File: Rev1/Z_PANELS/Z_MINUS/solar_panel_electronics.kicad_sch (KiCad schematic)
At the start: 34 parts, among them U3 LTC3130EUDC-1-PBF

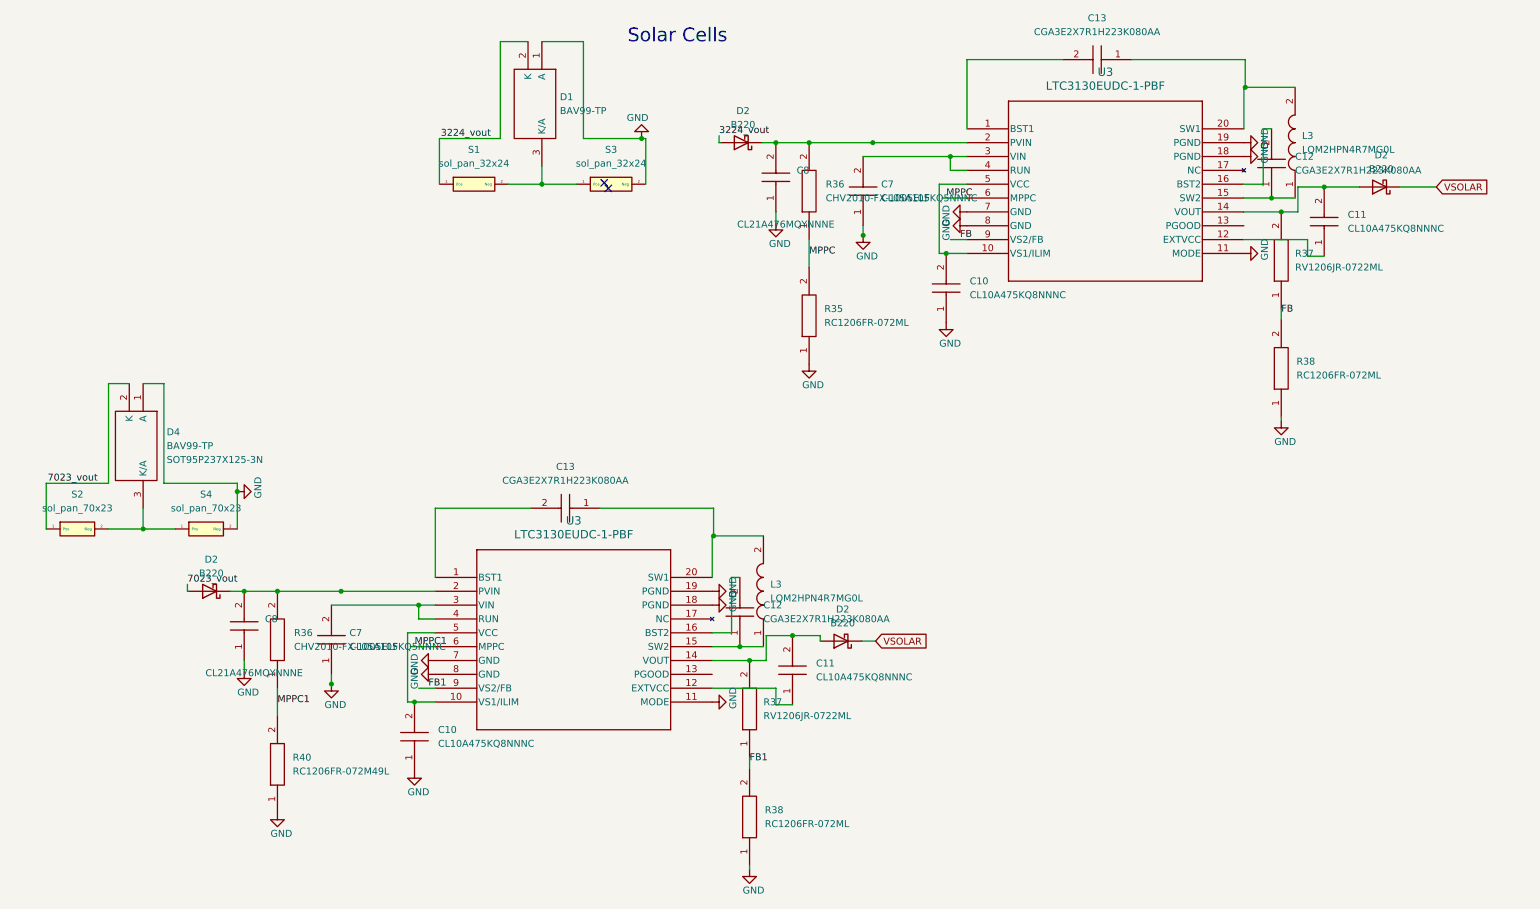
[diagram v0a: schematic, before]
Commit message: changed resistor sizes;
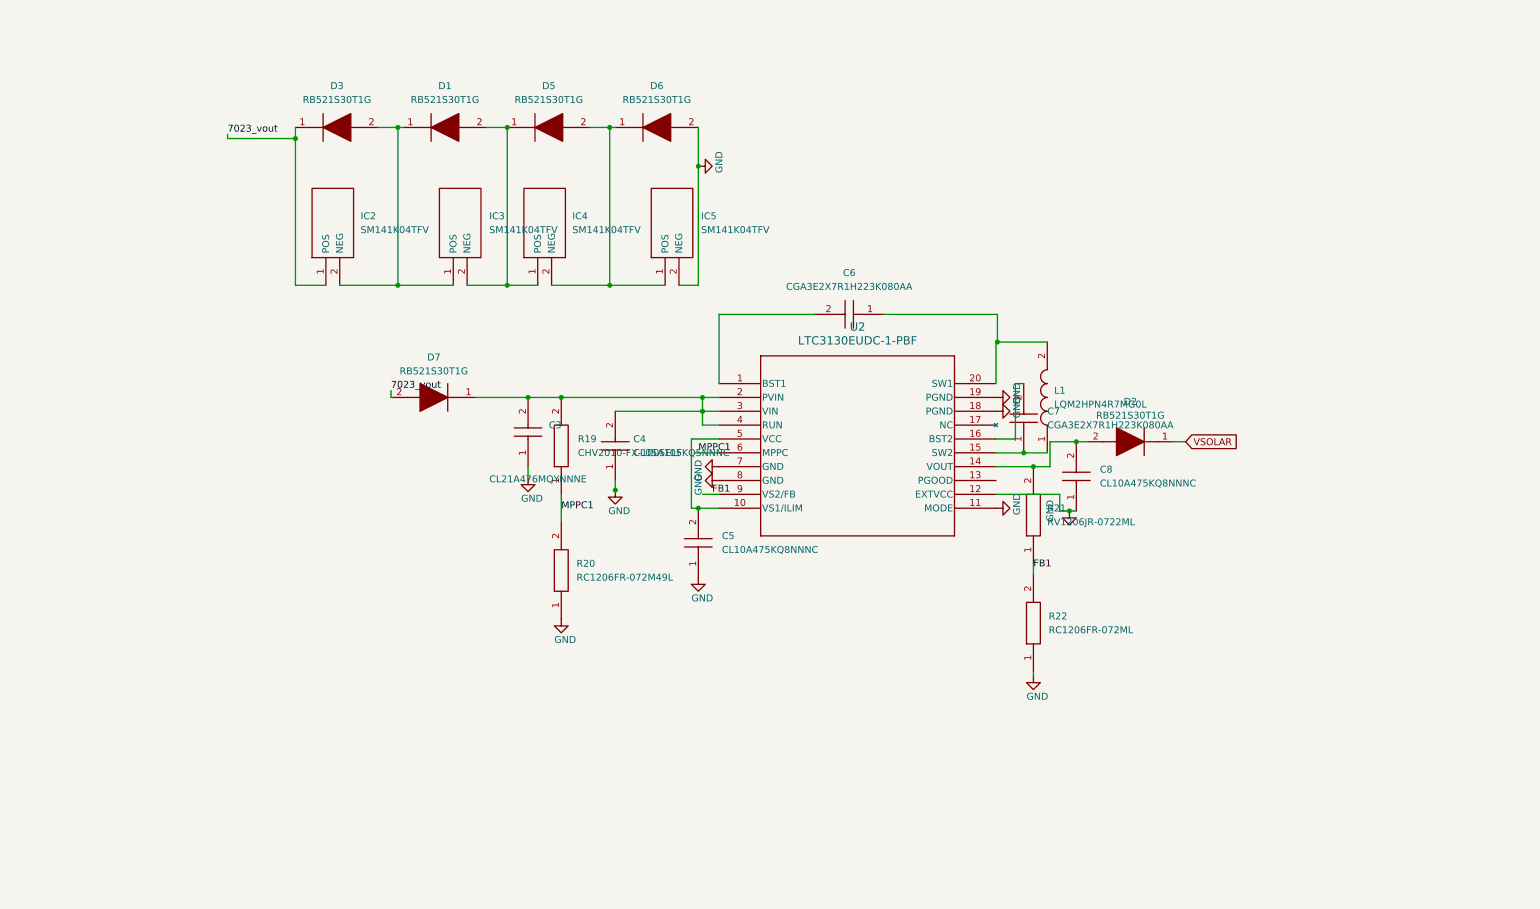
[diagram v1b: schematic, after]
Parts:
- removed C10 (x2), C11 (x2): CL10A475KQ8NNNC, CAPC1608X90N, symbol AA_AUTO_LOADER:CL10A475KQ8NNNC
- removed C12 (x2), C13 (x2): CGA3E2X7R1H223K080AA, CAPC1608X90N, symbol AA_AUTO_LOADER:CGA3E2X7R1H223K080AA
- removed C7 (x2): CL05A105KQ5NNNC, CAPC1005X55N, symbol AA_AUTO_LOADER:CL05A105KQ5NNNC
- removed C8 (x2): CL21A476MQYNNNE, CAPC2012X135N, symbol AA_AUTO_LOADER:CL21A476MQYNNNE
- removed D1, D4: BAV99-TP, SOT95P237X125-3N, symbol AA_AUTO_LOADER:BAV99-TP
- removed D2 (x4): B220, Diode_SMD:D_SMB, symbol Diode:B220
- removed L3 (x2): LQM2HPN4R7MG0L, LQM2HPN1R0MG0L, symbol AA_AUTO_LOADER:LQM2HPN4R7MG0L
- removed R35, R38 (x2): RC1206FR-072ML, RESC3116X65N, symbol AA_AUTO_LOADER:RC1206FR-072ML
- removed R36 (x2): CHV2010-FX-1005ELF, RESC5025X70N, symbol AA_AUTO_LOADER:CHV2010-FX-1005ELF
- removed R37 (x2): RV1206JR-0722ML, RESC3116X65N, symbol AA_AUTO_LOADER:RV1206JR-0722ML
- removed R40: RC1206FR-072M49L, RESC3116X65N, symbol AA_AUTO_LOADER:RC1206FR-072M49L
- removed S1, S3: sol_pan_32x24, CUSTOM_SOLAR_2432:solar_panel_SM500K12TF_32x24, symbol solar_symbol_lib:sol_pan_32x24
- removed S2, S4: sol_pan_70x23, CUSTOM_SOLAR_7023:sol_pan_SM141K10TFS_70x23, symbol solar_symbol_lib:sol_pan_70x23
- removed U3 (x2): LTC3130EUDC-1-PBF, UDC_20_ADI, symbol LTC3130:LTC3130EUDC-1-PBF
- added C3: CL21A476MQYNNNE, CAPC2012X135N, symbol AA_AUTO_LOADER:CL21A476MQYNNNE
- added C4: CL05A105KQ5NNNC, CAPC1005X55N, symbol AA_AUTO_LOADER:CL05A105KQ5NNNC
- added C5, C8: CL10A475KQ8NNNC, CAPC1608X90N, symbol AA_AUTO_LOADER:CL10A475KQ8NNNC
- added C6, C7: CGA3E2X7R1H223K080AA, CAPC1608X90N, symbol AA_AUTO_LOADER:CGA3E2X7R1H223K080AA
- added D1, D2, D3, D5, D6, D7: RB521S30T1G, SODFL1608X70N, symbol AA_AUTO_LOADER:RB521S30T1G
- added IC2, IC3, IC4, IC5: SM141K04TFV, SODFL490150X120N, symbol AA_AUTO_LOADER:SM141K04TFV
- added L1: LQM2HPN4R7MG0L, LQM2HPN1R0MG0L, symbol AA_AUTO_LOADER:LQM2HPN4R7MG0L
- added R19: CHV2010-FX-1005ELF, RESC5025X70N, symbol AA_AUTO_LOADER:CHV2010-FX-1005ELF
- added R20: RC1206FR-072M49L, RESC3116X65N, symbol AA_AUTO_LOADER:RC1206FR-072M49L
- added R21: RV1206JR-0722ML, RESC3116X65N, symbol AA_AUTO_LOADER:RV1206JR-0722ML
- added R22: RC1206FR-072ML, RESC3116X65N, symbol AA_AUTO_LOADER:RC1206FR-072ML
- added U2: LTC3130EUDC-1-PBF, UDC_20_ADI, symbol LTC3130:LTC3130EUDC-1-PBF
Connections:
- net 7023_vout: now also D3.1, D7.2, IC2.1 (POS)
- net FB1: now also R21.1, R22.2, U2.9 (VS2/FB)
- net GND: now also C3.1, C4.1, C5.1, C8.1, D6.2, IC5.2 (NEG), R20.1, R22.1, U2.11 (MODE), U2.12 (EXTVCC), U2.18 (PGND), U2.19 (PGND), U2.7 (GND), U2.8 (GND)
- net MPPC1: now also R19.1, R20.2, U2.6 (MPPC)
- net VSOLAR: now also D2.1
- new net: D1.1, D3.2, IC2.2 (NEG), IC3.1 (POS)
- new net: D1.2, D5.1, IC3.2 (NEG), IC4.1 (POS)
- new net: D5.2, D6.1, IC4.2 (NEG), IC5.1 (POS)
- new net: C7.1, L1.1, U2.15 (SW2)
- new net: C6.1, L1.2, U2.20 (SW1)
- new net: C5.2, U2.10 (VS1/ILIM), U2.5 (VCC)
- new net: C8.2, D2.2, R21.2, U2.14 (VOUT)
- new net: C3.2, C4.2, D7.1, R19.2, U2.2 (PVIN), U2.3 (VIN), U2.4 (RUN)
- new net: C6.2, U2.1 (BST1)
- new net: C7.2, U2.16 (BST2)
- no-connect marks 2 -> 0
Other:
- note removed: "Solar Cells"

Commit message: made changes to Z minus and Z plus cutouts
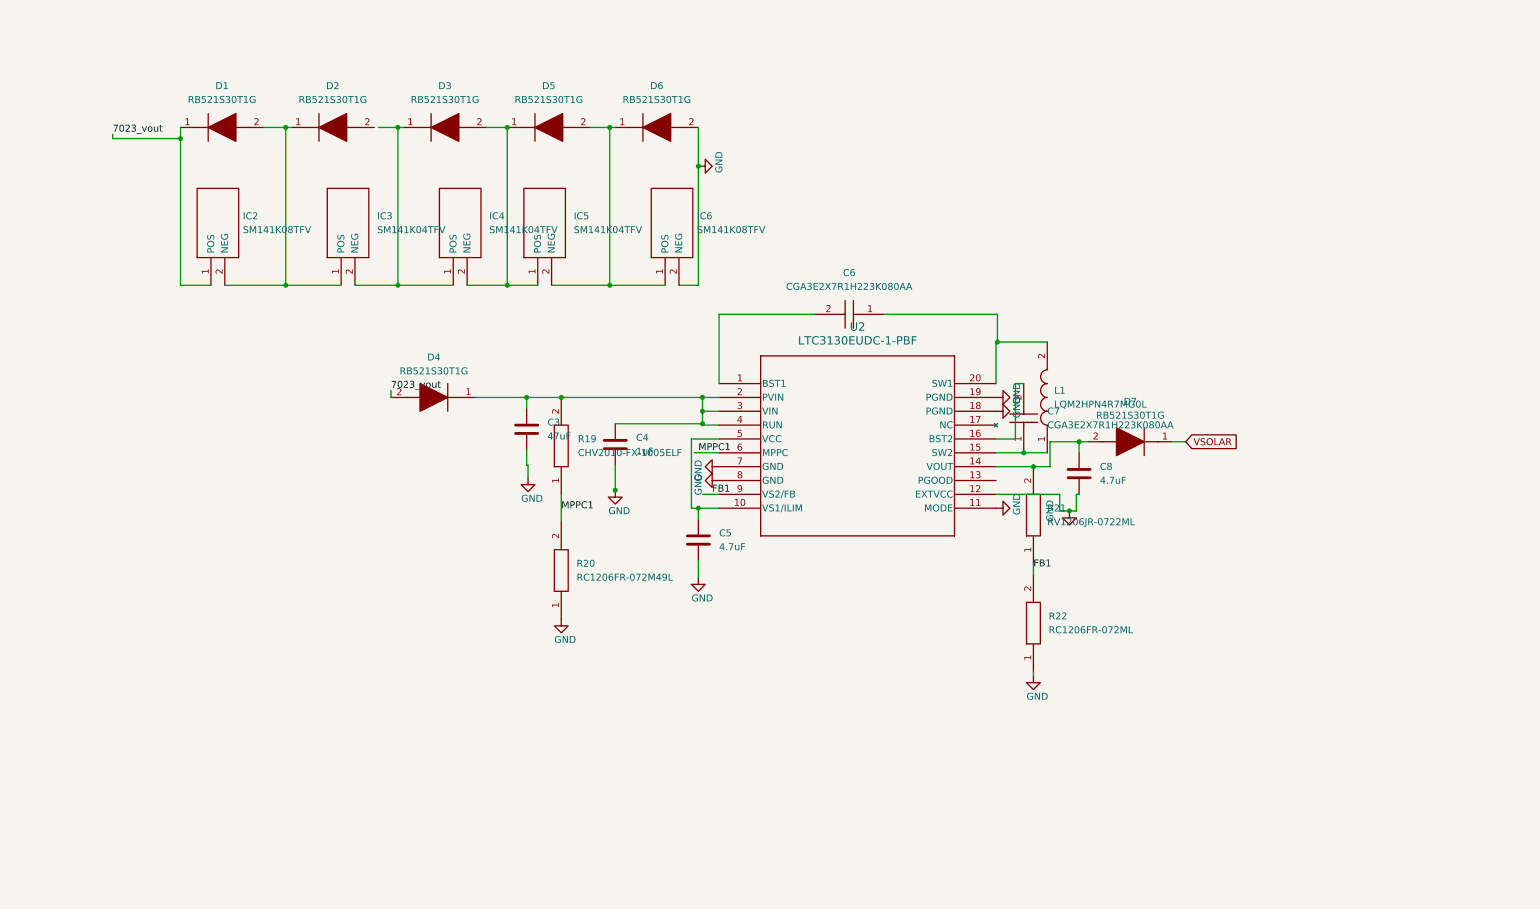
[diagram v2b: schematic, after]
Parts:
- removed C3: CL21A476MQYNNNE, CAPC2012X135N, symbol AA_AUTO_LOADER:CL21A476MQYNNNE
- removed C4: CL05A105KQ5NNNC, CAPC1005X55N, symbol AA_AUTO_LOADER:CL05A105KQ5NNNC
- removed C5, C8: CL10A475KQ8NNNC, CAPC1608X90N, symbol AA_AUTO_LOADER:CL10A475KQ8NNNC
- removed IC2: SM141K04TFV, SODFL490150X120N, symbol AA_AUTO_LOADER:SM141K04TFV
- added C3: 47uF, Capacitor_SMD:C_0805_2012Metric, symbol PCM_Capacitor_AKL:C_0805
- added C4: 1uF, Capacitor_SMD:C_0805_2012Metric, symbol PCM_Capacitor_AKL:C_0805
- added C5, C8: 4.7uF, Capacitor_SMD:C_0805_2012Metric, symbol PCM_Capacitor_AKL:C_0805
- added D2: RB521S30T1G, SODFL1608X70N, symbol AA_AUTO_LOADER:RB521S30T1G
- added IC2, IC6: SM141K08TFV, SODFL520290X120N, symbol AA_AUTO_LOADER:SM141K08TFV
- IC3, IC4, IC5: footprint SODFL490150X120N -> SODFL340230X120N
- renumbered D3 to D1, D1 to D3, D7 to D4, D2 to D7
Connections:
- net 7023_vout: now also IC2.1 (POS)
- net GND: now also C3.2, C4.2, C5.2, C8.2, IC6.2 (NEG); no longer IC5.2 (NEG)
- net at D1.2, IC3.1 (POS): now also D2.1, IC2.2 (NEG); no longer D3.1
- net at IC3.2 (NEG), IC4.1 (POS): now also D3.1; no longer D3.2, D5.1
- net at IC4.2 (NEG), IC5.1 (POS): now also D3.2, D5.1; no longer D5.2, D6.1
- net at U2.10 (VS1/ILIM), U2.5 (VCC): now also C5.1
- net at D7.2, R21.2, U2.14 (VOUT): now also C8.1
- net at D4.1, R19.2, U2.2 (PVIN)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: now also C3.1, C4.1
- new net: D5.2, D6.1, IC5.2 (NEG), IC6.1 (POS)
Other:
- moved on the sheet: D1
